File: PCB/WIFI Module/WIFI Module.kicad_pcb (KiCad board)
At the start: 4 copper layers, 23 x 13 mm, 18 parts, among them J1 Conn_01x01_Shielded, J2 Conn_02x04, U1 ESP8684, Y1 Q22FA12800230

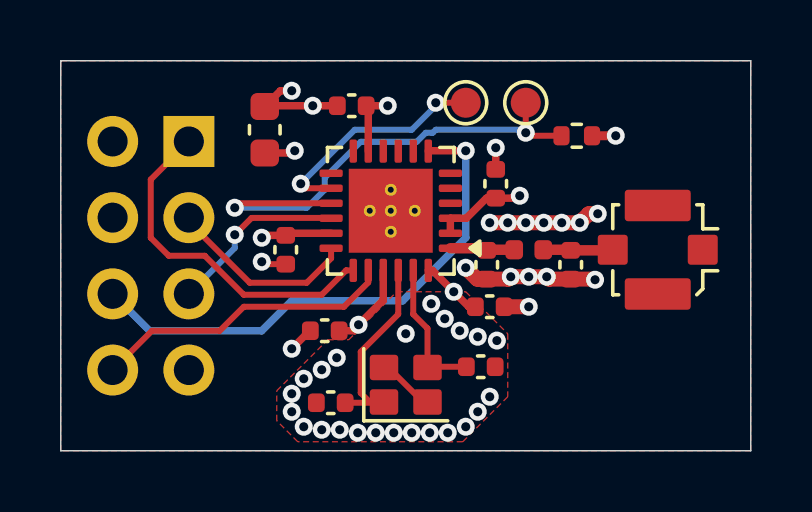
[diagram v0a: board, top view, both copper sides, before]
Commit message: Updated the PCB Allot
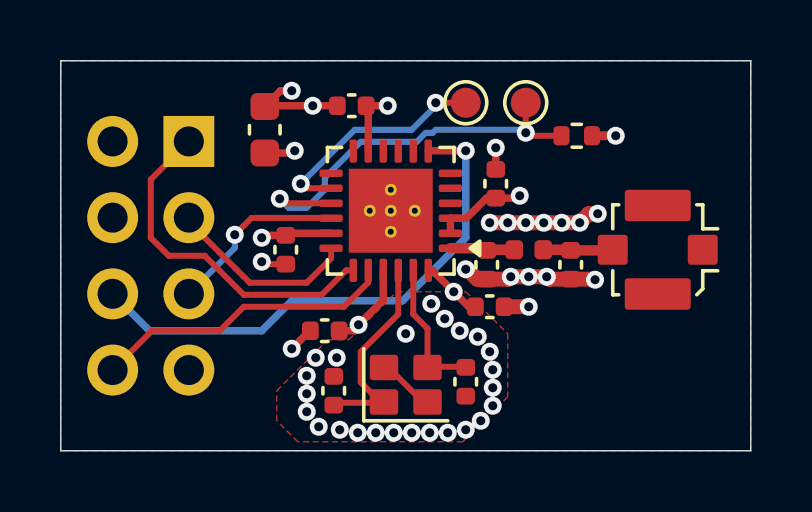
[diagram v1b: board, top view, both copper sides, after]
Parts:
- moved C10 0.71 mm to (133.5, 101.7), turned to 90 degrees
- moved C9 0.41 mm to (129.1, 102.0), turned to -90 degrees
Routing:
- net /GPIO9: track 16.6 -> 13.7 mm
- net GND: vias 41 -> 42
